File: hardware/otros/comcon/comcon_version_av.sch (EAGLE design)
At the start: 121 parts, among them IC1 74LS32N, IC10 74LS365N, IC11 74LS365N, IC12 74LS365N, IC13 74LS365N, IC14 74LS365N, IC7 74LS365N, IC8 74LS365N, IC9 74LS365N

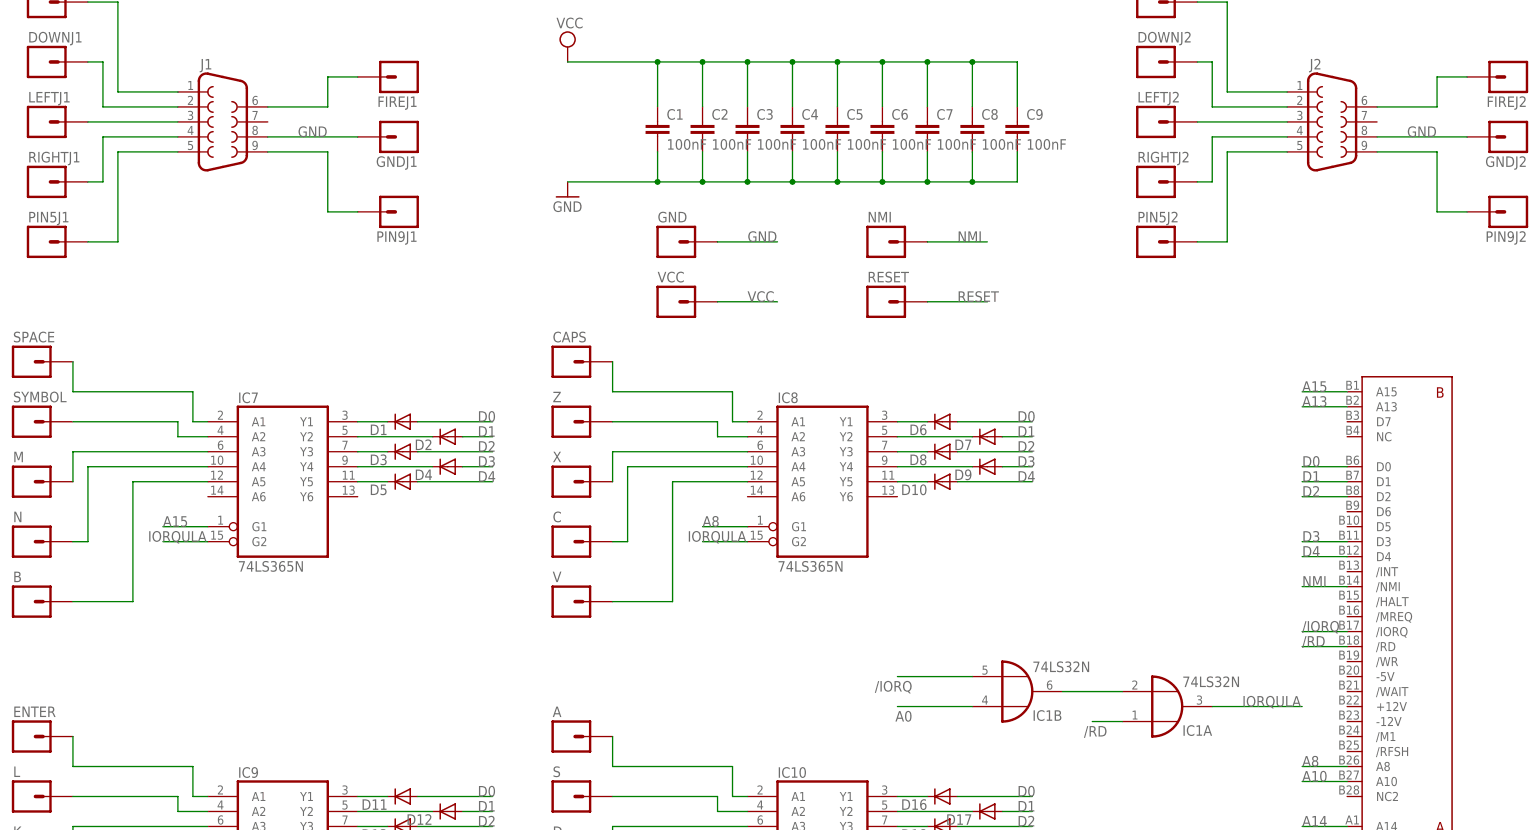
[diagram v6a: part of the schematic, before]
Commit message: Conecto VCC a conectores de Joystick y mejoro la serigrafía
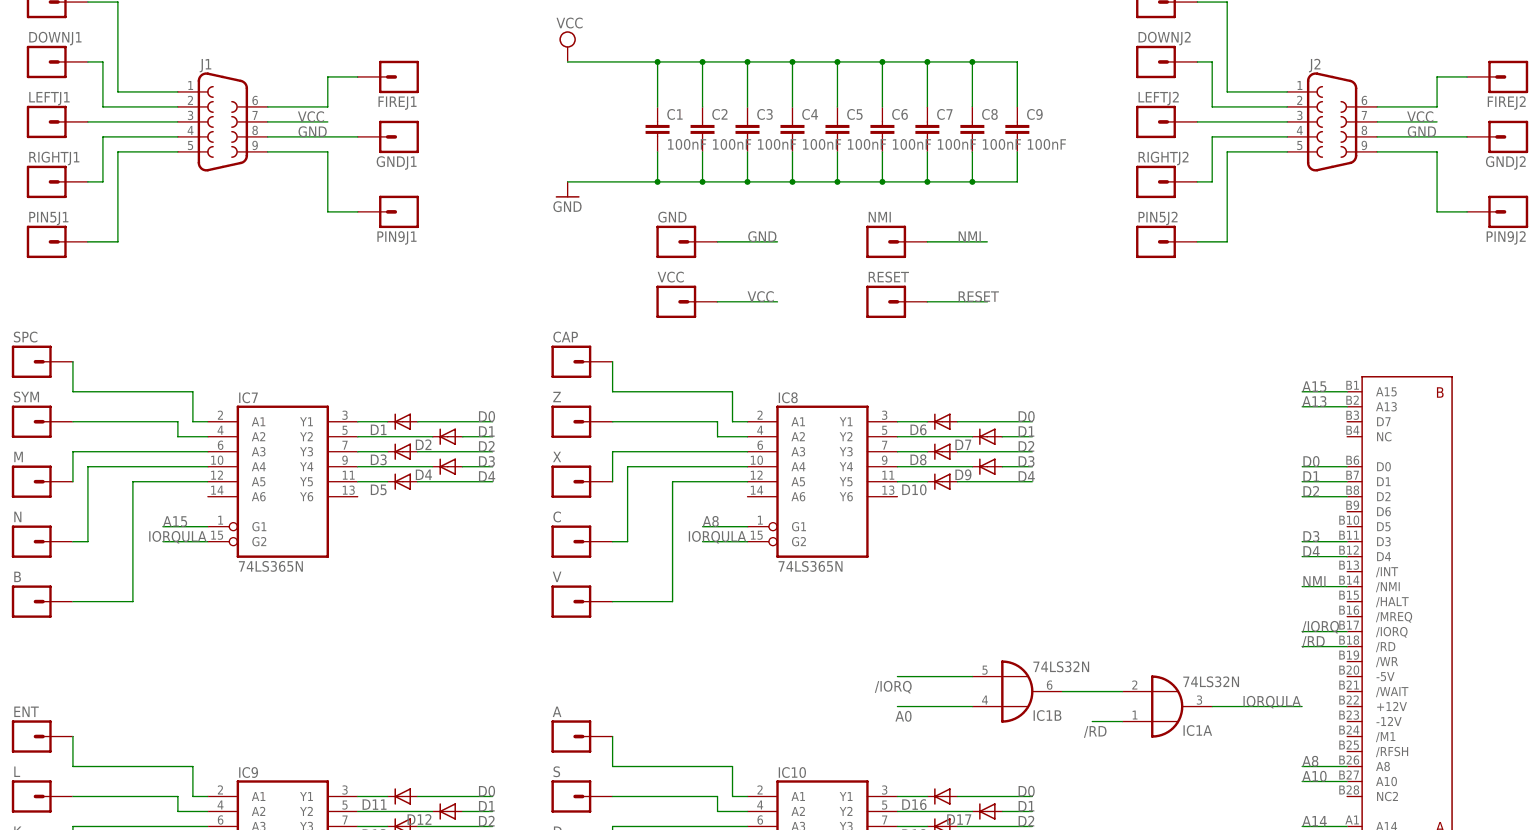
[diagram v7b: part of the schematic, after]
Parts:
- renumbered CAPS to CAP, ENTER to ENT, SPACE to SPC, SYMBOL to SYM
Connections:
- net VCC: now also J1.7, J2.7
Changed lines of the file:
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@@
 <part name="C6" library="rcl" deviceset="C-EU" device="050-025X075" value="100nF"/>
 <part name="IC7" library="74xx-eu" deviceset="74*365" device="N" technology="HC" value="74LS365N"/>
-<part name="SPACE" library="SparkFun-Connectors" deviceset="M01" device="PTH" value=""/>
-<part name="SYMBOL" library="SparkFun-Connectors" deviceset="M01" device="PTH" value=""/>
+<part name="SPC" library="SparkFun-Connectors" deviceset="M01" device="PTH" value=""/>
+<part name="SYM" library="SparkFun-Connectors" deviceset="M01" device="PTH" value=""/>
 <part name="M" library="SparkFun-Connectors" deviceset="M01" device="PTH" value=""/>
 <part name="N" library="SparkFun-Connectors" deviceset="M01" device="PTH" value=""/>
@@
 <part name="D5" library="diode" deviceset="1N4148" device="DO35-7" value=""/>
 <part name="IC8" library="74xx-eu" deviceset="74*365" device="N" technology="HC" value="74LS365N"/>
-<part name="CAPS" library="SparkFun-Connectors" deviceset="M01" device="PTH" value=""/>
+<part name="CAP" library="SparkFun-Connectors" deviceset="M01" device="PTH" value=""/>
 <part name="Z" library="SparkFun-Connectors" deviceset="M01" device="PTH" value=""/>
 <part name="X" library="SparkFun-Connectors" deviceset="M01" device="PTH" value=""/>
@@
 <part name="D10" library="diode" deviceset="1N4148" device="DO35-7" value=""/>
 <part name="IC9" library="74xx-eu" deviceset="74*365" device="N" technology="HC" value="74LS365N"/>
-<part name="ENTER" library="SparkFun-Connectors" deviceset="M01" device="PTH" value=""/>
+<part name="ENT" library="SparkFun-Connectors" deviceset="M01" device="PTH" value=""/>
 <part name="L" library="SparkFun-Connectors" deviceset="M01" device="PTH" value=""/>
 <part name="K" library="SparkFun-Connectors" deviceset="M01" device="PTH" value=""/>
@@
 <instance part="C6" gate="G$1" x="116.84" y="142.24"/>
 <instance part="IC7" gate="A" x="15.24" y="81.28"/>
-<instance part="SPACE" gate="G$1" x="-27.94" y="101.6"/>
-<instance part="SYMBOL" gate="G$1" x="-27.94" y="91.44"/>
+<instance part="SPC" gate="G$1" x="-27.94" y="101.6"/>
+<instance part="SYM" gate="G$1" x="-27.94" y="91.44"/>
 <instance part="M" gate="G$1" x="-27.94" y="81.28"/>
 <instance part="N" gate="G$1" x="-27.94" y="71.12"/>
@@
 <instance part="D5" gate="G$1" x="35.56" y="81.28" rot="R180"/>
 <instance part="IC8" gate="A" x="106.68" y="81.28"/>
-<instance part="CAPS" gate="G$1" x="63.5" y="101.6"/>
+<instance part="CAP" gate="G$1" x="63.5" y="101.6"/>
 <instance part="Z" gate="G$1" x="63.5" y="91.44"/>
 <instance part="X" gate="G$1" x="63.5" y="81.28"/>
@@
 <instance part="D10" gate="G$1" x="127" y="81.28" rot="R180"/>
 <instance part="IC9" gate="A" x="15.24" y="17.78"/>
-<instance part="ENTER" gate="G$1" x="-27.94" y="38.1"/>
+<instance part="ENT" gate="G$1" x="-27.94" y="38.1"/>
 <instance part="L" gate="G$1" x="-27.94" y="27.94"/>
 <instance part="K" gate="G$1" x="-27.94" y="17.78"/>
@@
 <label x="93.98" y="111.76" size="1.778" layer="95"/>
 </segment>
+<segment>
+<pinref part="J2" gate="G$1" pin="7"/>
+<wire x1="200.66" y1="142.24" x2="210.82" y2="142.24" width="0.1524" layer="91"/>
+<label x="205.74" y="142.24" size="1.778" layer="95"/>
+</segment>
+<segment>
+<pinref part="J1" gate="G$1" pin="7"/>
+<wire x1="12.7" y1="142.24" x2="22.86" y2="142.24" width="0.1524" layer="91"/>
+<label x="17.78" y="142.24" size="1.778" layer="95"/>
+</segment>
 </net>
 <net name="A14" class="0">
@@
 <wire x1="0" y1="96.52" x2="0" y2="91.44" width="0.1524" layer="91"/>
 <wire x1="0" y1="91.44" x2="2.54" y2="91.44" width="0.1524" layer="91"/>
-<pinref part="SPACE" gate="G$1" pin="1"/>
+<pinref part="SPC" gate="G$1" pin="1"/>
 <wire x1="-20.32" y1="101.6" x2="-20.32" y2="96.52" width="0.1524" layer="91"/>
 <wire x1="-20.32" y1="96.52" x2="0" y2="96.52" width="0.1524" layer="91"/>
@@
 <wire x1="-2.54" y1="91.44" x2="-2.54" y2="88.9" width="0.1524" layer="91"/>
 <wire x1="-2.54" y1="88.9" x2="2.54" y2="88.9" width="0.1524" layer="91"/>
-<pinref part="SYMBOL" gate="G$1" pin="1"/>
+<pinref part="SYM" gate="G$1" pin="1"/>
 <wire x1="-20.32" y1="91.44" x2="-2.54" y2="91.44" width="0.1524" layer="91"/>
 </segment>
@@
 <wire x1="91.44" y1="96.52" x2="91.44" y2="91.44" width="0.1524" layer="91"/>
 <wire x1="91.44" y1="91.44" x2="93.98" y2="91.44" width="0.1524" layer="91"/>
-<pinref part="CAPS" gate="G$1" pin="1"/>
+<pinref part="CAP" gate="G$1" pin="1"/>
 <wire x1="71.12" y1="101.6" x2="71.12" y2="96.52" width="0.1524" layer="91"/>
 <wire x1="71.12" y1="96.52" x2="91.44" y2="96.52" width="0.1524" layer="91"/>
@@
 <wire x1="0" y1="33.02" x2="0" y2="27.94" width="0.1524" layer="91"/>
 <wire x1="0" y1="27.94" x2="2.54" y2="27.94" width="0.1524" layer="91"/>
-<pinref part="ENTER" gate="G$1" pin="1"/>
+<pinref part="ENT" gate="G$1" pin="1"/>
 <wire x1="-20.32" y1="38.1" x2="-20.32" y2="33.02" width="0.1524" layer="91"/>
 <wire x1="-20.32" y1="33.02" x2="0" y2="33.02" width="0.1524" layer="91"/>

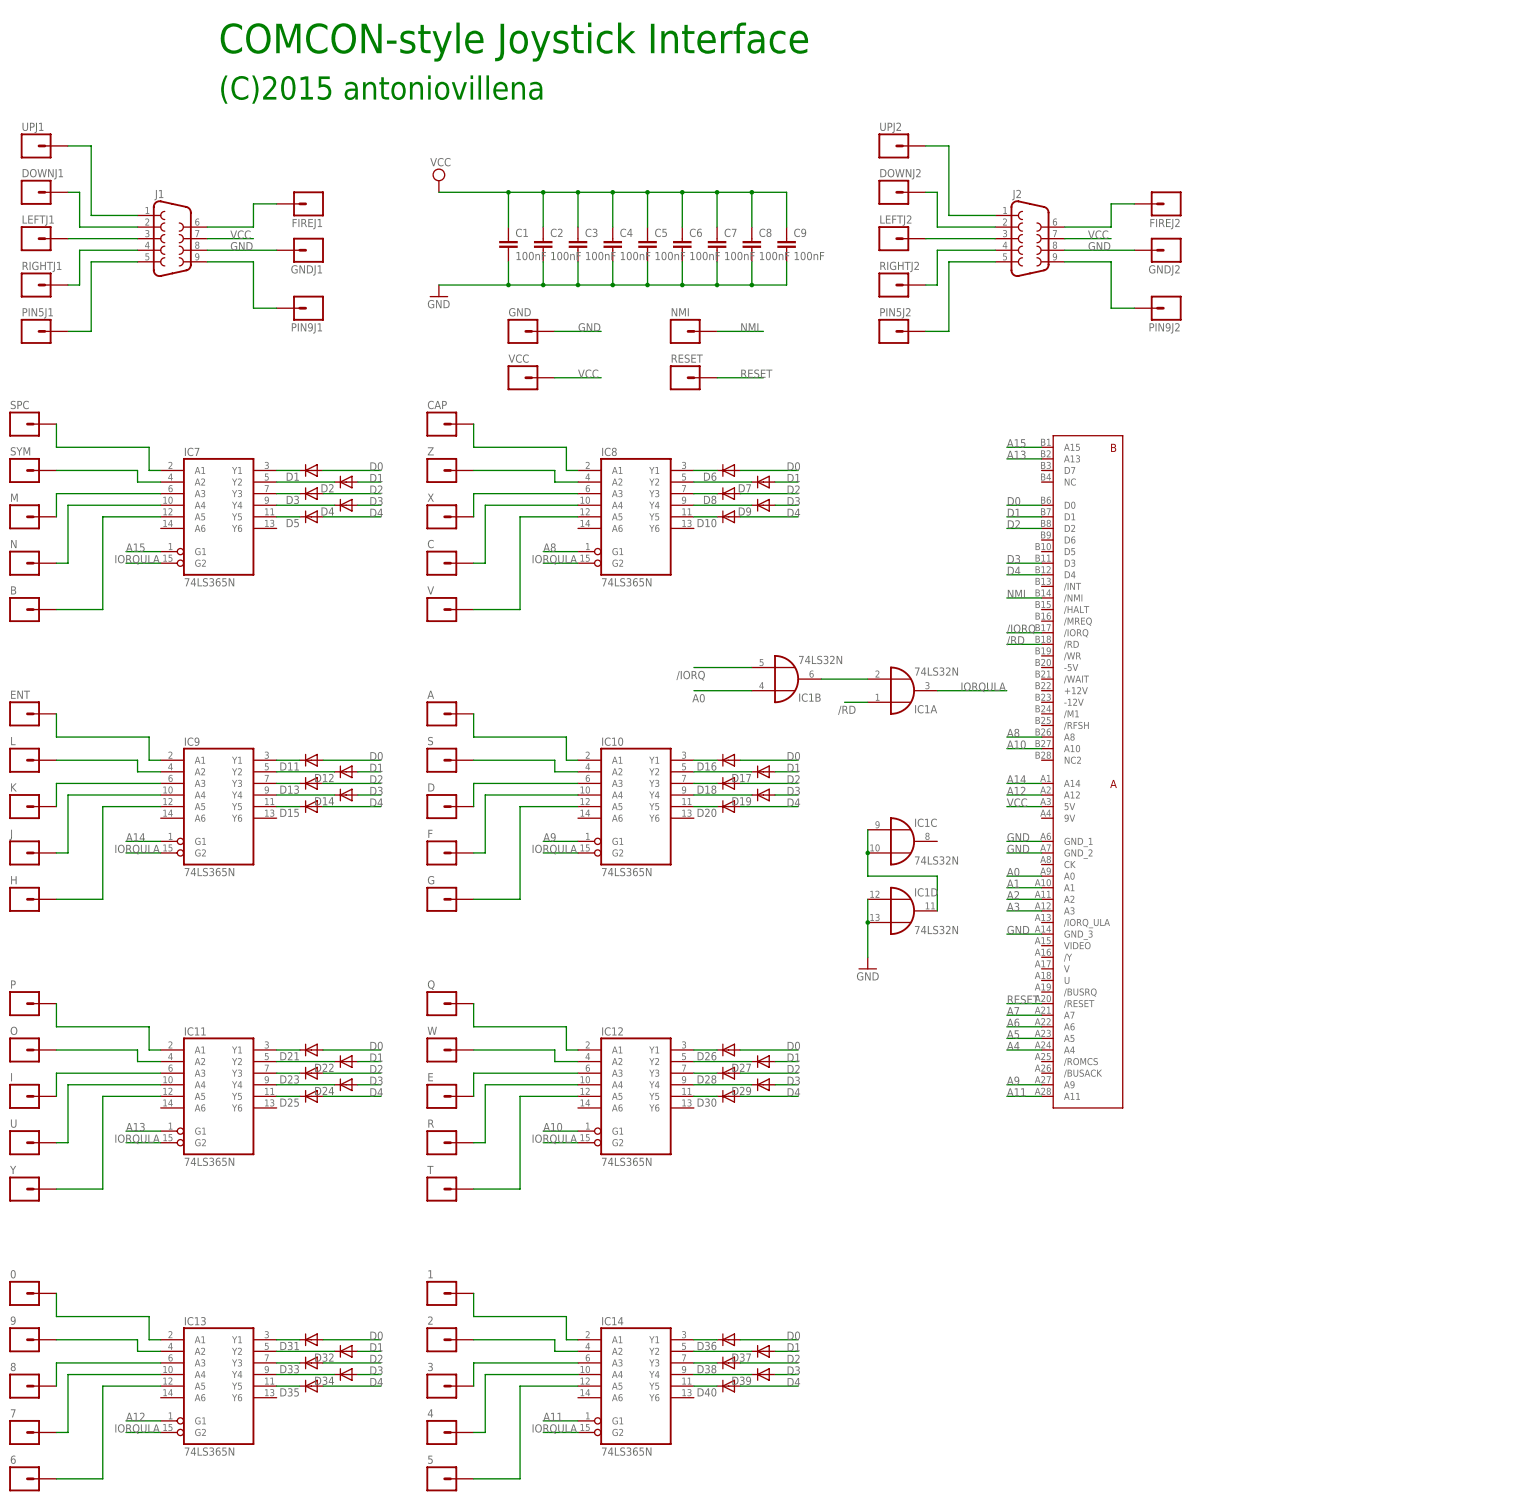
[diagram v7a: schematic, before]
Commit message: 
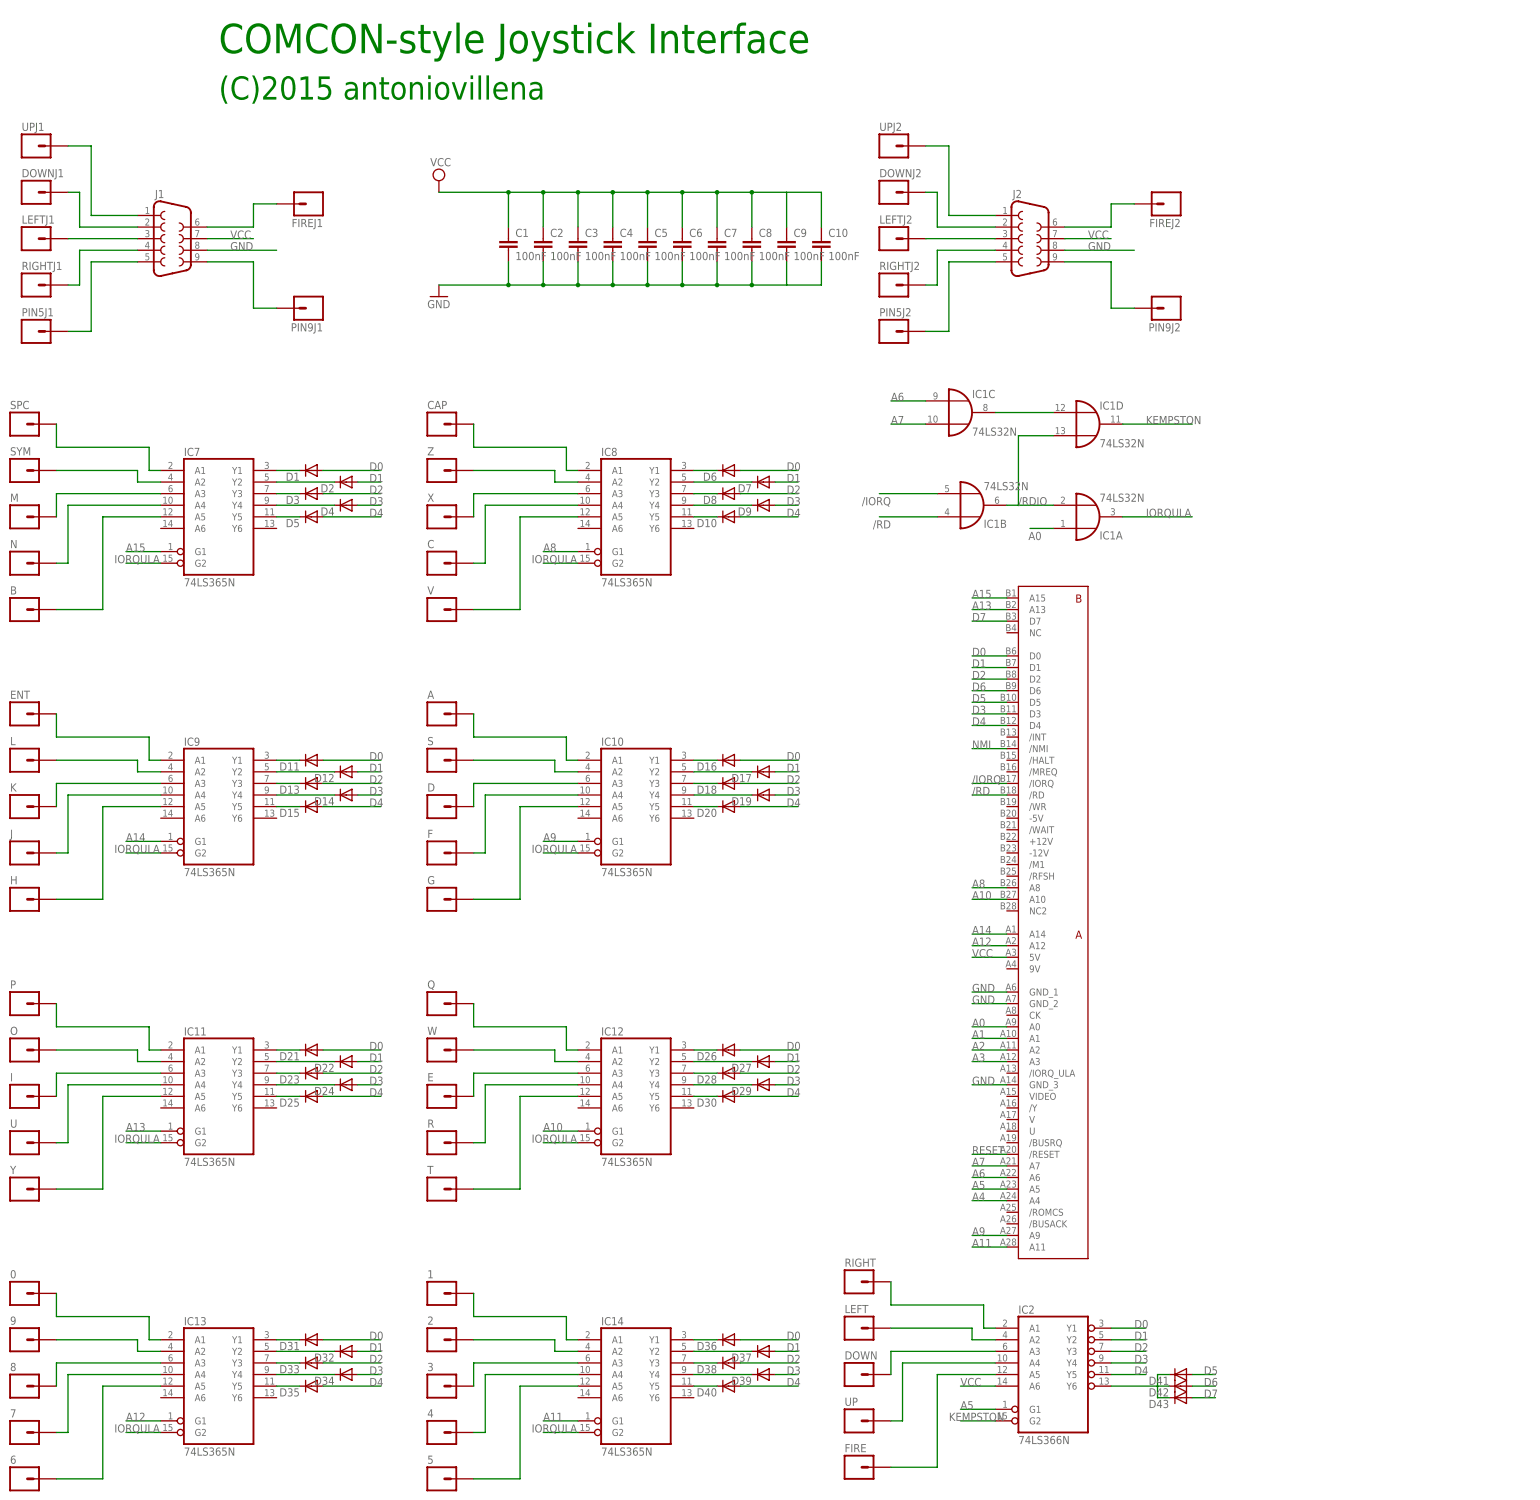
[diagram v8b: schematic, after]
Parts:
- removed GND, GNDJ1, GNDJ2, NMI, RESET, VCC: M01PTH, SparkFun-Connectors:M01PTH
- added C10: 100nF, rcl:C-EU050-025X075
- added D41, D42, D43: 1N4148DO35-7, diode:1N4148DO35-7
- added DOWN, FIRE, LEFT, RIGHT, UP: M01PTH, SparkFun-Connectors:M01PTH
- added IC2: 74LS366N, 74xx-eu:74LS366N
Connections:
- removed net N$4: IC1C.I0, IC1C.I1, IC1D.O
- new net /RDIO: IC1A.I1, IC1B.O, IC1D.I1
- new net D5: D41.A, U$3.D5
- new net D6: D42.A, U$3.D6
- new net D7: D43.A, U$3.D7
- new net KEMPSTON: IC1D.O, IC2A.G2
- new net N$32: IC1C.O, IC1D.I0
- new net N$36: IC2A.A1, RIGHT.1
- new net N$37: IC2A.A2, LEFT.1
- new net N$38: DOWN.1, IC2A.A3
- new net N$39: IC2A.A4, UP.1
- new net N$40: FIRE.1, IC2A.A5
- net /RD: now also IC1B.I0; no longer IC1A.I0
- net A0: now also IC1A.I0; no longer IC1B.I0
- net A5: now also IC2A.G1
- net A6: now also IC1C.I0
- net A7: now also IC1C.I1
- net D0: now also IC2A.Y1
- net D1: now also IC2A.Y2
- net D2: now also IC2A.Y3
- net D3: now also IC2A.Y4
- net D4: now also IC2A.Y5
- net GND: now also C10.2; no longer GND.1, GNDJ1.1, GNDJ2.1, IC1D.I0, IC1D.I1
- net N$1: now also D41.C, D42.C, D43.C, IC2A.Y6; no longer IC1A.I1, IC1B.O
- net NMI: no longer NMI.1
- net RESET: no longer RESET.1
- net VCC: now also C10.1, IC2A.A6; no longer VCC.1
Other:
- moved on the sheet: IC1A, IC1B, IC1C, IC1D
